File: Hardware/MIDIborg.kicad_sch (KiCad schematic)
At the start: 42 parts

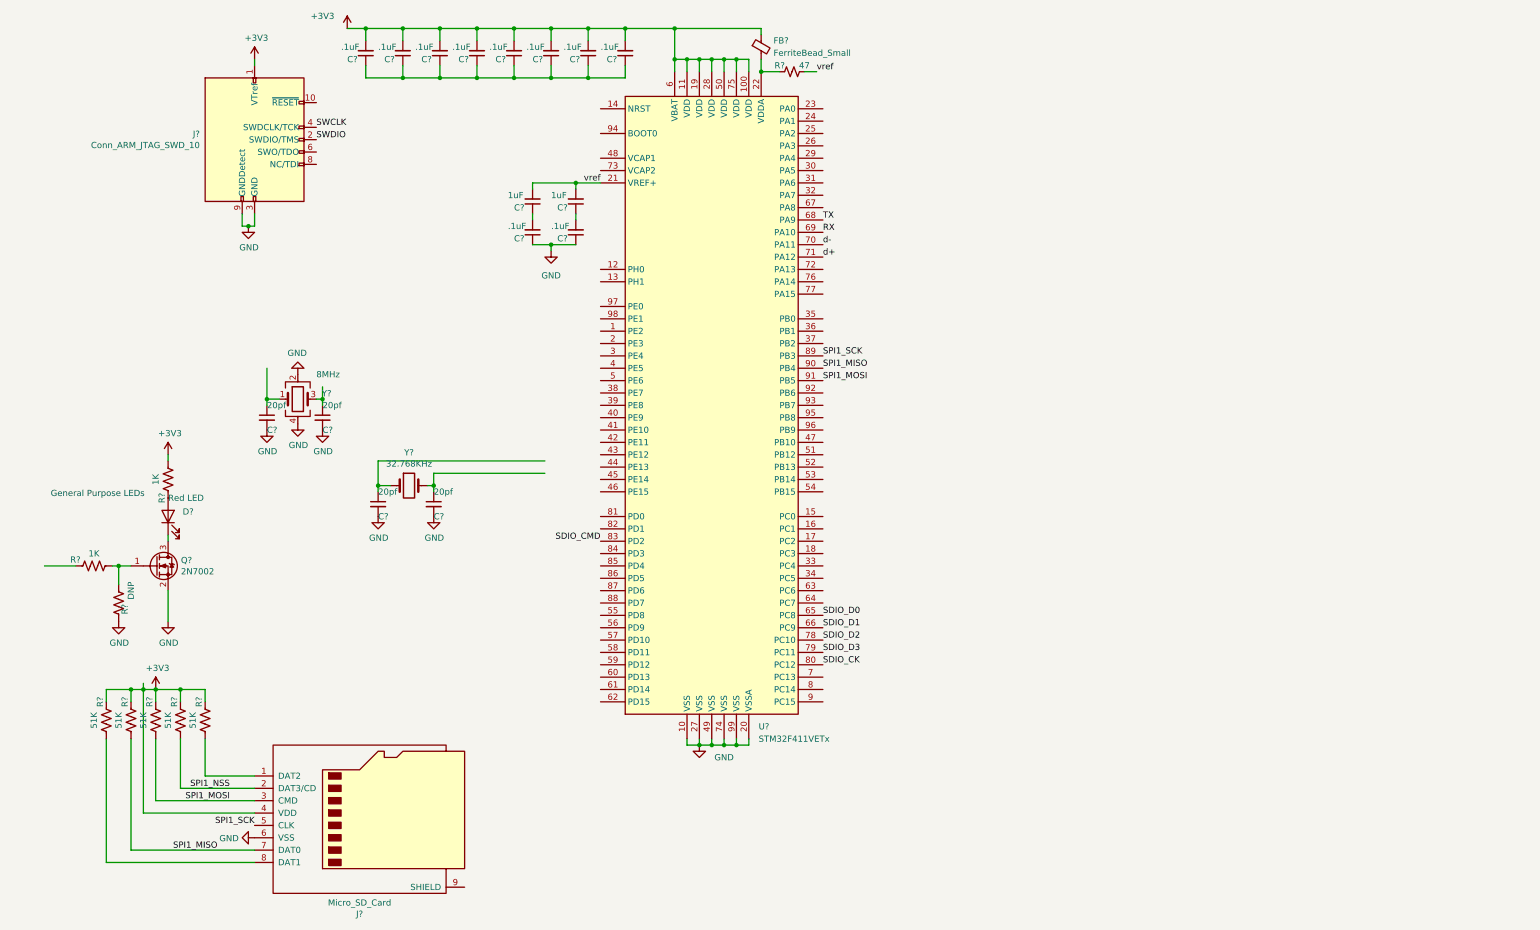
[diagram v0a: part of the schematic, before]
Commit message: Transition to RP2040
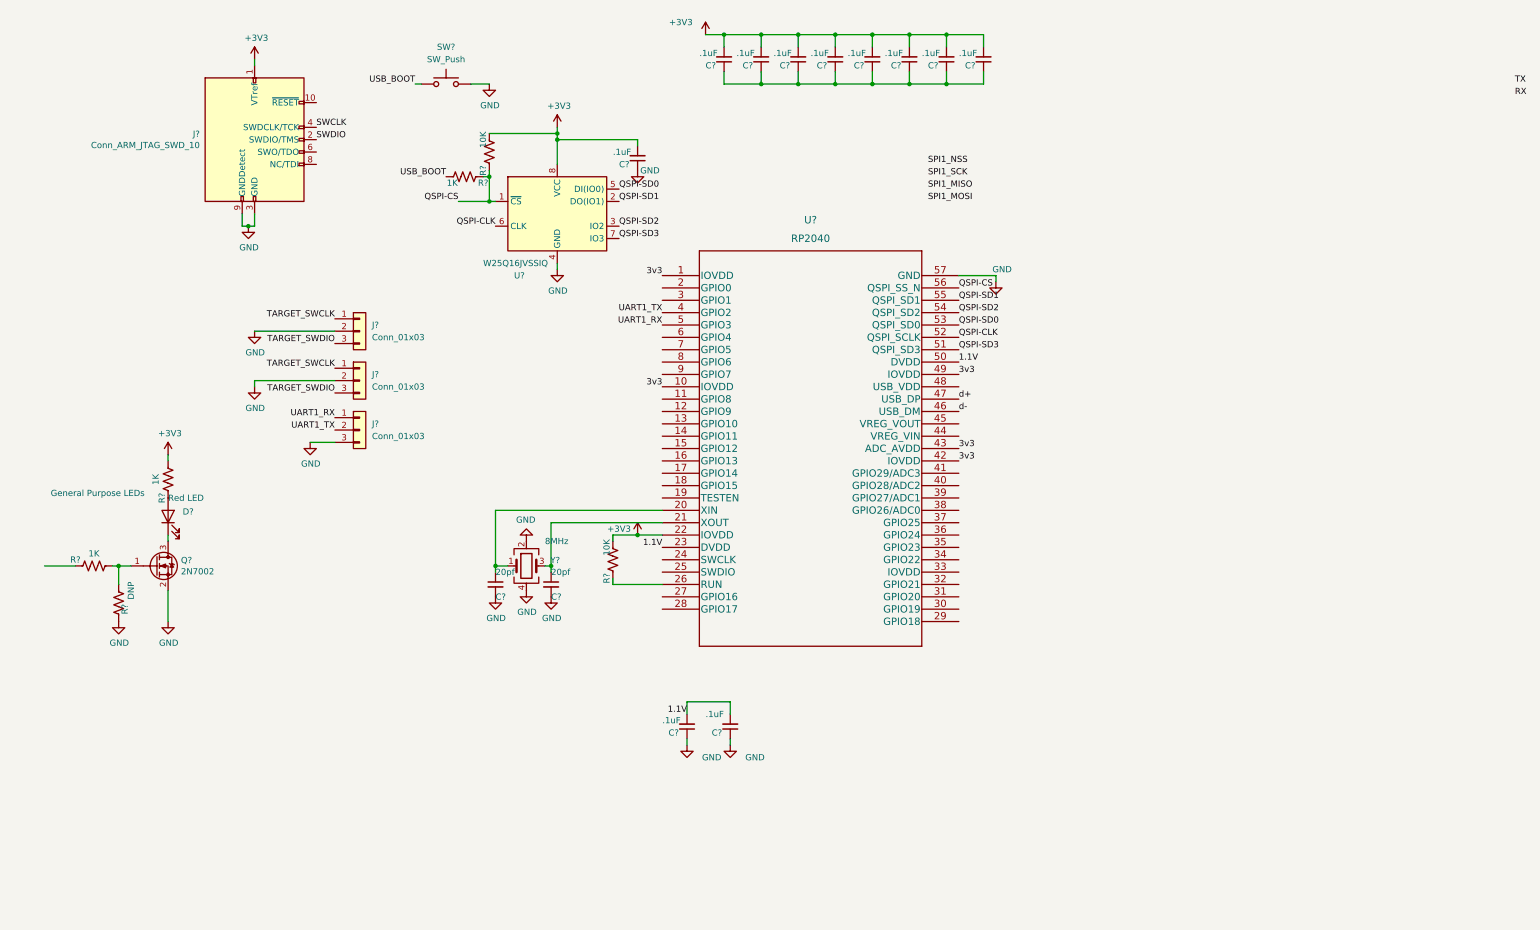
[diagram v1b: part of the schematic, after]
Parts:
- removed C? (x3): .1uF, Capacitor_SMD:C_0402_1005Metric_Pad0.74x0.62mm_HandSolder, symbol Device:C_Small
- removed C? (x2): 20pf, Inductor_SMD:L_0402_1005Metric, symbol Device:C_Small
- removed C? (x2): 1uF, Capacitor_SMD:C_0805_2012Metric_Pad1.18x1.45mm_HandSolder, symbol Device:C_Small
- removed FB?: FerriteBead_Small, symbol Device:FerriteBead_Small
- removed J?: Micro_SD_Card, Connector_Card:microSD_HC_Hirose_DM3AT-SF-PEJM5, symbol Connector:Micro_SD_Card
- removed R? (x5): 51K, Resistor_SMD:R_0402_1005Metric_Pad0.72x0.64mm_HandSolder, symbol Device:R_US
- removed R?: 47, Resistor_SMD:R_0402_1005Metric_Pad0.72x0.64mm_HandSolder, symbol Device:R_Small_US
- removed U?: STM32F411VETx, Package_QFP:LQFP-100_14x14mm_P0.5mm, symbol MCU_ST_STM32F4:STM32F411VETx
- removed Y?: 32.768KHz, Crystal:Crystal_SMD_3215-2Pin_3.2x1.5mm, symbol Device:Crystal
- added C? (x4): .1uF, Capacitor_SMD:C_0402_1005Metric_Pad0.74x0.62mm_HandSolder, symbol Device:C_Small
- added J? (x3): Conn_01x03, symbol Connector_Generic:Conn_01x03
- added R?: 1K, Resistor_SMD:R_0402_1005Metric_Pad0.72x0.64mm_HandSolder, symbol Device:R_US
- added R? (x2): 10K, Resistor_SMD:R_0402_1005Metric_Pad0.72x0.64mm_HandSolder, symbol Device:R_US
- added SW?: SW_Push, symbol Switch:SW_Push
- added U?: RP2040, IC57_RP2040, symbol RP2040:RP2040
- added U?: W25Q16JVSSIQ, Package_SO:SOIC-8_5.23x5.23mm_P1.27mm, symbol Memory_Flash:W25Q32JVSS
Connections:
- net +3V3: now also C?.2, C?.2, C?.2, R?.1, R?.1, U?.22 (IOVDD), U?.8 (VCC); no longer C?.2
- net GND: now also C?.1, C?.1, C?.1, J?.2 (Pin_2), J?.2 (Pin_2), J?.3 (Pin_3), SW?.2, U?.4 (GND), U?.57 (GND)
- net d+: now also U?.47 (USB_DP)
- net d-: now also U?.46 (USB_DM)
- net at C?.1, C?.1, C?.1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: now also C?.1, C?.1; no longer C?.1
- net at C?.1, Y?.1: now also U?.20 (XIN)
- net at C?.1, Y?.3: now also U?.21 (XOUT)
- new net: R?.2, U?.26 (RUN)
- new net 1.1V: C?.2, C?.2, U?.23 (DVDD), U?.50 (DVDD)
- new net 3v3: U?.1 (IOVDD), U?.10 (IOVDD), U?.42 (IOVDD), U?.43 (ADC_AVDD), U?.49 (IOVDD)
- new net QSPI-CLK: U?.52 (QSPI_SCLK), U?.6 (CLK)
- new net QSPI-CS: R?.2, R?.2, U?.1 (~{CS}), U?.56 (QSPI_SS_N)
- new net QSPI-SD0: U?.5 (DI(IO0)), U?.53 (QSPI_SD0)
- new net QSPI-SD1: U?.2 (DO(IO1)), U?.55 (QSPI_SD1)
- new net QSPI-SD2: U?.3 (IO2), U?.54 (QSPI_SD2)
- new net QSPI-SD3: U?.51 (QSPI_SD3), U?.7 (IO3)
- new net TARGET_SWCLK: J?.1 (Pin_1), J?.1 (Pin_1)
- new net TARGET_SWDIO: J?.3 (Pin_3), J?.3 (Pin_3)
- new net UART1_RX: J?.1 (Pin_1), U?.5 (GPIO3)
- new net UART1_TX: J?.2 (Pin_2), U?.4 (GPIO2)
- new net USB_BOOT: R?.1, SW?.1
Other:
- moved on the sheet: C?, Y?

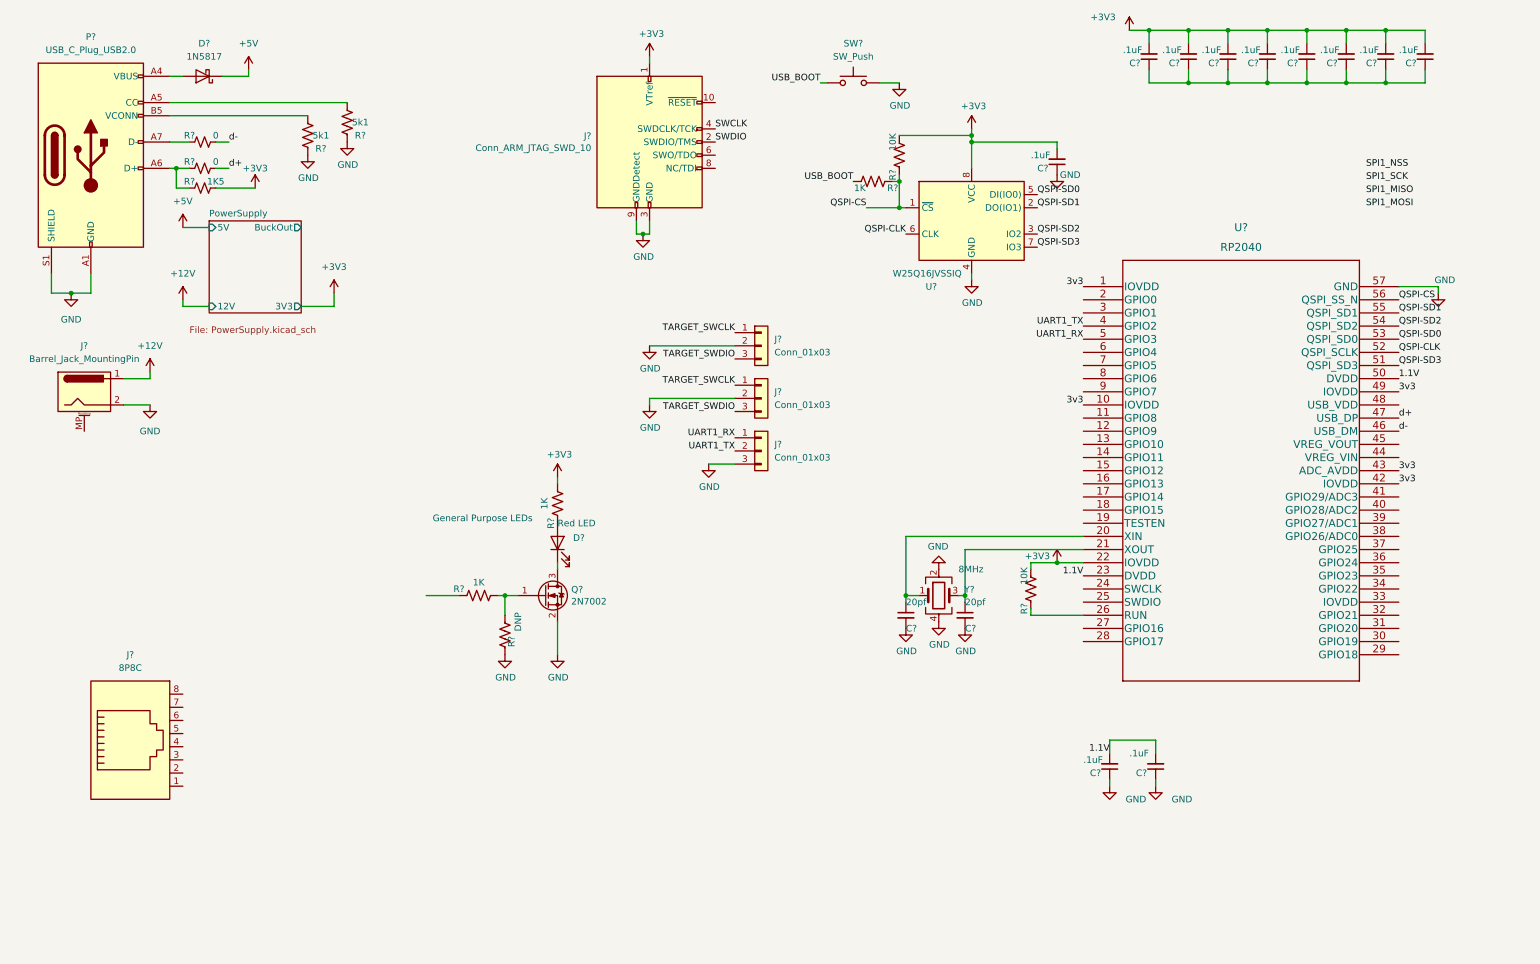
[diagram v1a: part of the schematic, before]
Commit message: Finished Schematics and placed most components
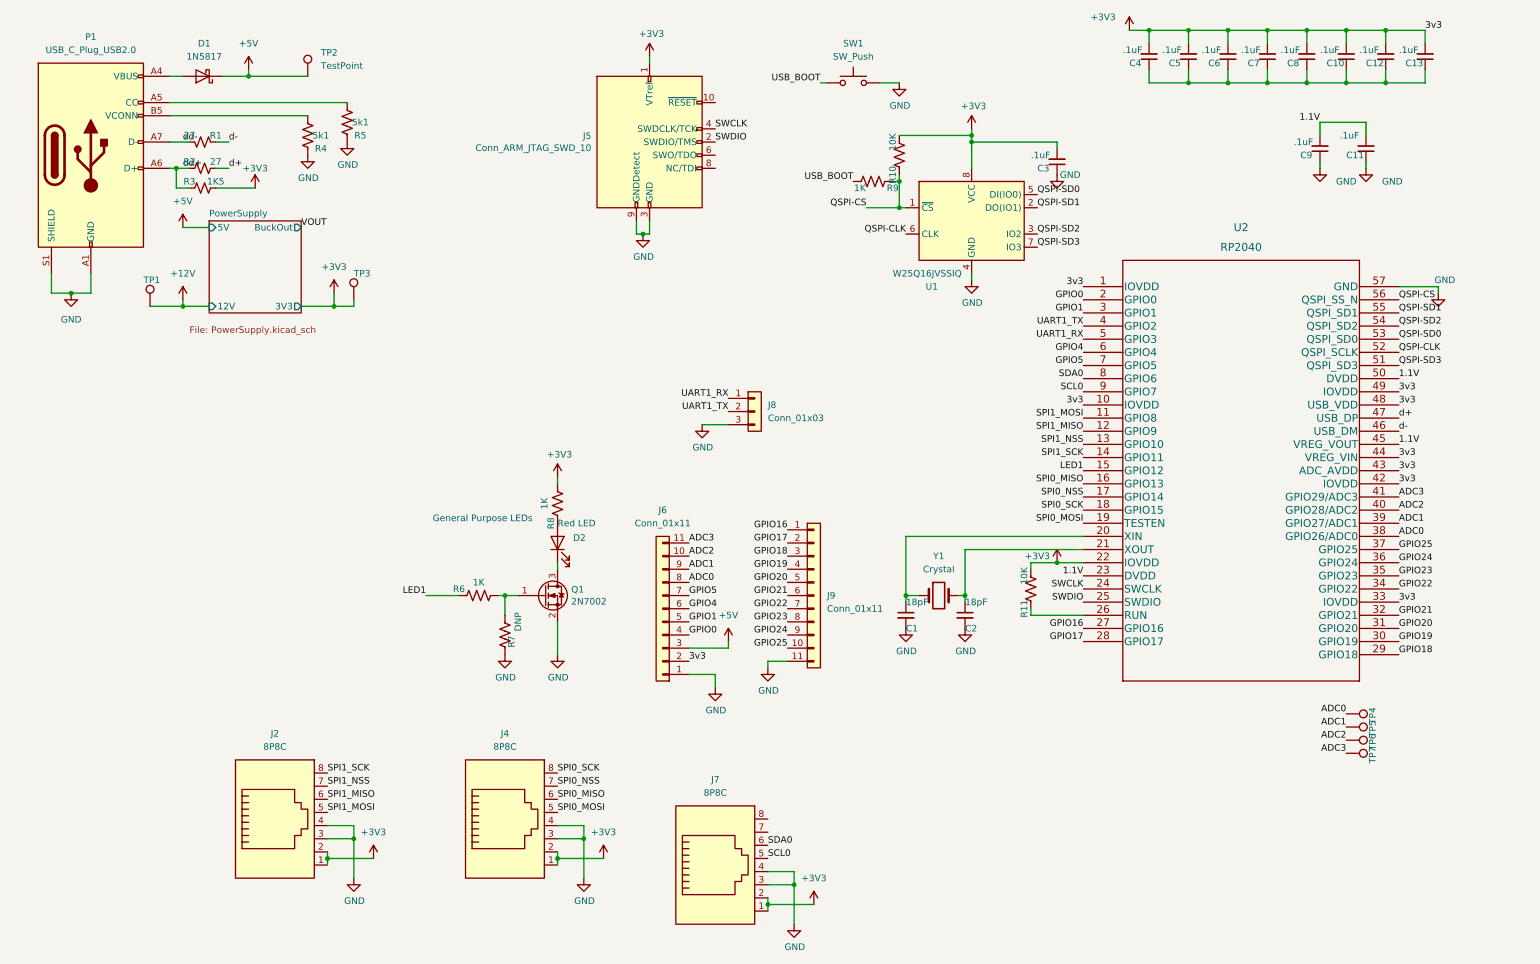
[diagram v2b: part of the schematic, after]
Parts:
- removed J? (x2): Conn_01x03, symbol Connector_Generic:Conn_01x03
- removed J?: Barrel_Jack_MountingPin, Connector_BarrelJack:BarrelJack_CUI_PJ-063AH_Horizontal, symbol Connector:Barrel_Jack_MountingPin
- removed Y?: 8MHz, Crystal:Crystal_SMD_5032-4Pin_5.0x3.2mm, symbol Device:Crystal_GND24
- added J4, J7: 8P8C, Connector_RJ:RJ45_OST_PJ012-8P8CX_Vertical, symbol Connector:8P8C
- added J6, J9: Conn_01x11, Connector_PinHeader_2.54mm:PinHeader_1x11_P2.54mm_Vertical_SMD_Pin1Left, symbol Connector_Generic:Conn_01x11
- added TP1, TP2, TP3, TP4, TP5, TP6, TP7: TestPoint, TestPoint:TestPoint_Pad_D1.5mm, symbol Connector:TestPoint
- added Y1: Crystal, Crystal:Crystal_HC49-4H_Vertical, symbol Device:Crystal
- C1, C2: renamed from C?; value 20pf -> 18pF
- J2: renamed from J?; footprint (none) -> Connector_RJ:RJ45_OST_PJ012-8P8CX_Vertical
- J8: renamed from J?; footprint (none) -> Connector_PinHeader_2.54mm:PinHeader_1x03_P2.54mm_Vertical
- P1: renamed from P?; footprint (none) -> Connector_USB:USB_C_Receptacle_XKB_U262-16XN-4BVC11
- R1, R2: renamed from R?; value 0 -> 27
- SW1: renamed from SW?; footprint (none) -> Button_Switch_SMD:SW_Push_1P1T_NO_Vertical_Wuerth_434133025816
- U2: renamed from U?; footprint IC57_RP2040 -> Package_DFN_QFN:QFN-56-1EP_8x8mm_P0.5mm_EP4.3x4.3mm
- gave numbers to parts that had none: 25
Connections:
- net 3v3 is gone; now on net +3V3: U2.1 (IOVDD), U2.10 (IOVDD), U2.42 (IOVDD), U2.43 (ADC_AVDD), U2.49 (IOVDD)
- net +12V: now also TP1.1
- net +3V3: now also J2.1, J2.2, U2.33 (IOVDD), U2.44 (VREG_VIN), U2.48 (USB_VDD), J4.1, J4.2, J6.2 (Pin_2), J7.1, J7.2, TP3.1
- net +5V: now also J6.3 (Pin_3), TP2.1
- net 1.1V: now also U2.45 (VREG_VOUT)
- net GND: now also J2.3, J2.4, J4.3, J4.4, J6.1 (Pin_1), J7.3, J7.4, J9.11 (Pin_11)
- net SPI1_MISO: now also J2.6, U2.12 (GPIO9)
- net SPI1_MOSI: now also J2.5, U2.11 (GPIO8)
- net SPI1_NSS: now also J2.7, U2.13 (GPIO10)
- net SPI1_SCK: now also J2.8, U2.14 (GPIO11)
- net SWCLK: now also U2.24 (SWCLK)
- net SWDIO: now also U2.25 (SWDIO)
- net d-: now also R1.2; no longer R1.1
- net at C1.1, U2.20 (XIN): now also Y1.1
- net at C2.1, U2.21 (XOUT): now also Y1.2
- net LED1: now reaches U2.15 (GPIO12)
- net LED1: now also R6.2
- net SPI0_MISO: now reaches U2.16 (GPIO13)
- net SPI0_MISO: now also J4.6
- net SPI0_NSS: now reaches U2.17 (GPIO14)
- net SPI0_NSS: now also J4.7
- net SPI0_SCK: now reaches U2.18 (GPIO15)
- net SPI0_SCK: now also J4.8
- net SPI0_MOSI: now reaches U2.19 (TESTEN)
- net SPI0_MOSI: now also J4.5
- net GPIO0: now reaches U2.2 (GPIO0)
- net GPIO0: now also J6.4 (Pin_4)
- net GPIO16: now reaches U2.27 (GPIO16)
- net GPIO16: now also J9.1 (Pin_1)
- net GPIO17: now reaches U2.28 (GPIO17)
- net GPIO17: now also J9.2 (Pin_2)
- net GPIO18: now reaches U2.29 (GPIO18)
- net GPIO18: now also J9.3 (Pin_3)
- net GPIO1: now reaches U2.3 (GPIO1)
- net GPIO1: now also J6.5 (Pin_5)
- net GPIO19: now reaches U2.30 (GPIO19)
- net GPIO19: now also J9.4 (Pin_4)
- net GPIO20: now reaches U2.31 (GPIO20)
- net GPIO20: now also J9.5 (Pin_5)
- net GPIO21: now reaches U2.32 (GPIO21)
- net GPIO21: now also J9.6 (Pin_6)
- net GPIO22: now reaches U2.34 (GPIO22)
- net GPIO22: now also J9.7 (Pin_7)
- net GPIO23: now reaches U2.35 (GPIO23)
- net GPIO23: now also J9.8 (Pin_8)
- net GPIO24: now reaches U2.36 (GPIO24)
- net GPIO24: now also J9.9 (Pin_9)
- net GPIO25: now reaches U2.37 (GPIO25)
- net GPIO25: now also J9.10 (Pin_10)
- net ADC0: now reaches U2.38 (GPIO26/ADC0)
- net ADC0: now also J6.8 (Pin_8), TP4.1
- net ADC1: now reaches U2.39 (GPIO27/ADC1)
- net ADC1: now also J6.9 (Pin_9), TP5.1
- net ADC2: now reaches U2.40 (GPIO28/ADC2)
- net ADC2: now also J6.10 (Pin_10), TP6.1
- net ADC3: now reaches U2.41 (GPIO29/ADC3)
- net ADC3: now also J6.11 (Pin_11), TP7.1
- net GPIO4: now reaches U2.6 (GPIO4)
- net GPIO4: now also J6.6 (Pin_6)
- net GPIO5: now reaches U2.7 (GPIO5)
- net GPIO5: now also J6.7 (Pin_7)
- net SDA0: now reaches U2.8 (GPIO6)
- net SDA0: now also J7.6
- net SCL0: now reaches U2.9 (GPIO7)
- net SCL0: now also J7.5
- net dd+: now reaches P1.A6 (D+), R2.2, R3.2
- net dd-: now reaches P1.A7 (D-)
- net dd-: now also R1.1; no longer R1.2
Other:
- moved on the sheet: C11, C9, J2, J8, R1
